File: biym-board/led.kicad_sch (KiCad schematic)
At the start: 0 parts

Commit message: Wire led sheet
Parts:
- added J?: HEADER_01X04_JST_PH_VERTICAL, Janelia:JST_PH_B4B-PH-K_1x04_P2.00mm_Vertical, symbol Janelia:HEADER_01X04_JST_PH_VERTICAL
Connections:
- new net CKI: J?.3 (Pin_3)
- new net GND: J?.1 (Pin_1)
- new net SDI: J?.2 (Pin_2)
- new net VLED: J?.4 (Pin_4)
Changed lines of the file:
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@@
 (kicad_sch (version 20211123) (generator eeschema)
   (paper "A4")
+  (wire (pts (xy 124.46 88.9) (xy 127 88.9))
+    (stroke (width 0) (type default) (color 0 0 0 0))
+  )
+  (wire (pts (xy 124.46 91.44) (xy 127 91.44))
+    (stroke (width 0) (type default) (color 0 0 0 0))
+  )
+  (wire (pts (xy 124.46 86.36) (xy 127 86.36))
+    (stroke (width 0) (type default) (color 0 0 0 0))
+  )
+  (wire (pts (xy 124.46 93.98) (xy 127 93.98))
+    (stroke (width 0) (type default) (color 0 0 0 0))
+  )
+  (hierarchical_label "VLED" (shape passive) (at 124.46 86.36 180)
+    (effects (font (size 1.27 1.27)) (justify right))
+  )
+  (hierarchical_label "SDI" (shape input) (at 124.46 91.44 180)
+    (effects (font (size 1.27 1.27)) (justify right))
+  )
+  (hierarchical_label "GND" (shape passive) (at 124.46 93.98 180)
+    (effects (font (size 1.27 1.27)) (justify right))
+  )
+  (hierarchical_label "CKI" (shape input) (at 124.46 88.9 180)
+    (effects (font (size 1.27 1.27)) (justify right))
+  )
+  (symbol (lib_id "Janelia:HEADER_01X04_JST_PH_VERTICAL") (at 132.08 90.17 180) (unit 1)
+    (in_bom yes) (on_board yes)
+    (property "Reference" "J?" (id 0) (at 132.08 83.82 0))
+    (property "Value" "HEADER_01X04_JST_PH_VERTICAL" (id 1) (at 134.62 90.17 90))
+    (property "Footprint" "Janelia:JST_PH_B4B-PH-K_1x04_P2.00mm_Vertical" (id 2) (at 132.08 102.87 0)
+      (effects (font (size 1.27 1.27)) hide)
+    )
+    (property "Datasheet" "" (id 3) (at 132.08 91.44 0)
+      (effects (font (size 1.27 1.27)) hide)
+    )
+    (property "Description" "CONN HEADER VERT 4POS 2MM" (id 4) (at 132.08 100.33 0)
+      (effects (font (size 1.27 1.27)) hide)
+    )
+    (property "Manufacturer" "JST Sales America Inc." (id 5) (at 132.08 107.95 0)
+      (effects (font (size 1.27 1.27)) hide)
+    )
+    (property "Manufacturer Part Number" "B4B-PH-K-S(LF)(SN)" (id 6) (at 132.08 105.41 0)
+      (effects (font (size 1.27 1.27)) hide)
+    )
+    (property "Vendor" "Digi-Key" (id 7) (at 132.08 110.49 0)
+      (effects (font (size 1.27 1.27)) hide)
+    )
+    (property "Vendor Part Number" "455-1706-ND" (id 8) (at 132.08 113.03 0)
+      (effects (font (size 1.27 1.27)) hide)
+    )
+    (pin "1")
+    (pin "2")
+    (pin "3")
+    (pin "4")
+  )
 )

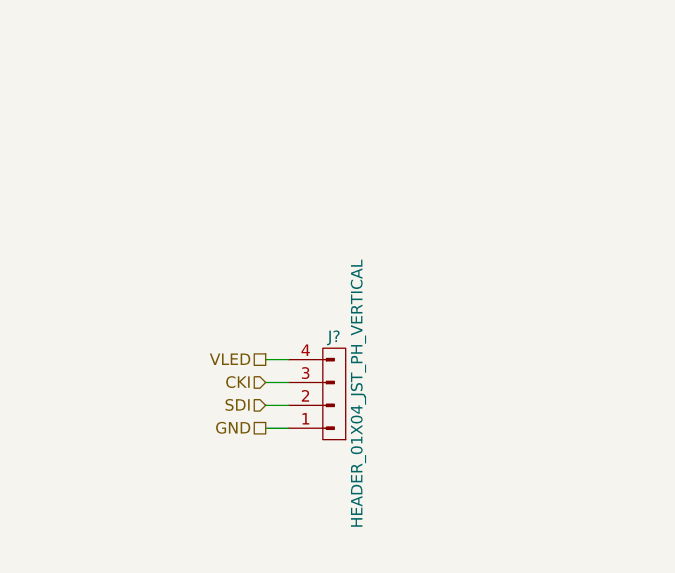
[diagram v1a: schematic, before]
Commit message: Add boosted voltage
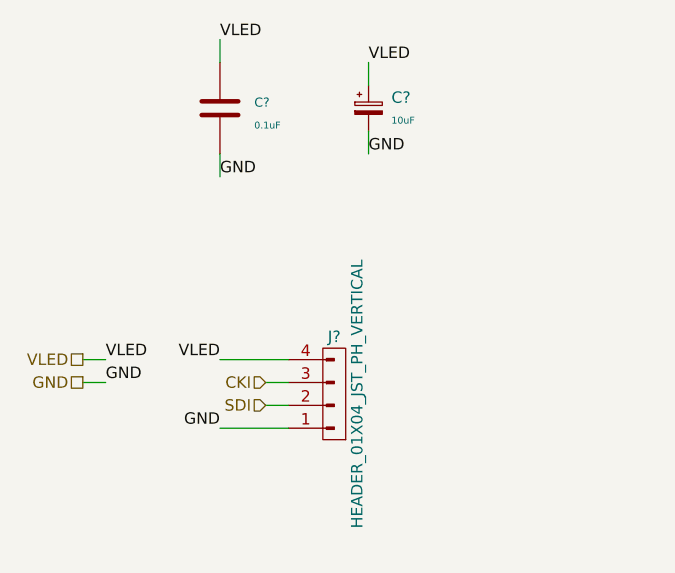
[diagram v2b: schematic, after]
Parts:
- added C?: 0.1uF, Janelia:SM0402, symbol Janelia:0.1uF_0402
- added C?: 10uF, Janelia:SM0402_POL, symbol Janelia:10uF_0402_POL
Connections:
- net GND: now also C?.2, C?.2
- net VLED: now also C?.1, C?.1
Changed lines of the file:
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@@
 (kicad_sch (version 20211123) (generator eeschema)
   (paper "A4")
+  (wire (pts (xy 119.38 63.5) (xy 119.38 66.04))
+    (stroke (width 0) (type default) (color 0 0 0 0))
+  )
+  (wire (pts (xy 135.89 60.96) (xy 135.89 63.5))
+    (stroke (width 0) (type default) (color 0 0 0 0))
+  )
   (wire (pts (xy 124.46 88.9) (xy 127 88.9))
+    (stroke (width 0) (type default) (color 0 0 0 0))
+  )
+  (wire (pts (xy 135.89 53.34) (xy 135.89 55.88))
+    (stroke (width 0) (type default) (color 0 0 0 0))
+  )
+  (wire (pts (xy 104.14 88.9) (xy 106.68 88.9))
+    (stroke (width 0) (type default) (color 0 0 0 0))
+  )
+  (wire (pts (xy 104.14 86.36) (xy 106.68 86.36))
     (stroke (width 0) (type default) (color 0 0 0 0))
   )
@@
     (stroke (width 0) (type default) (color 0 0 0 0))
   )
-  (wire (pts (xy 124.46 86.36) (xy 127 86.36))
+  (wire (pts (xy 119.38 50.8) (xy 119.38 53.34))
     (stroke (width 0) (type default) (color 0 0 0 0))
   )
-  (wire (pts (xy 124.46 93.98) (xy 127 93.98))
+  (wire (pts (xy 119.38 86.36) (xy 127 86.36))
     (stroke (width 0) (type default) (color 0 0 0 0))
   )
-  (hierarchical_label "VLED" (shape passive) (at 124.46 86.36 180)
+  (wire (pts (xy 119.38 93.98) (xy 127 93.98))
+    (stroke (width 0) (type default) (color 0 0 0 0))
+  )
+  (label "VLED" (at 135.89 53.34 0)
+    (effects (font (size 1.27 1.27)) (justify left bottom))
+  )
+  (label "VLED" (at 119.38 86.36 180)
+    (effects (font (size 1.27 1.27)) (justify right bottom))
+  )
+  (label "GND" (at 119.38 93.98 180)
+    (effects (font (size 1.27 1.27)) (justify right bottom))
+  )
+  (label "GND" (at 135.89 63.5 0)
+    (effects (font (size 1.27 1.27)) (justify left bottom))
+  )
+  (label "VLED" (at 106.68 86.36 0)
+    (effects (font (size 1.27 1.27)) (justify left bottom))
+  )
+  (label "VLED" (at 119.38 50.8 0)
+    (effects (font (size 1.27 1.27)) (justify left bottom))
+  )
+  (label "GND" (at 119.38 66.04 0)
+    (effects (font (size 1.27 1.27)) (justify left bottom))
+  )
+  (label "GND" (at 106.68 88.9 0)
+    (effects (font (size 1.27 1.27)) (justify left bottom))
+  )
+  (hierarchical_label "VLED" (shape passive) (at 104.14 86.36 180)
     (effects (font (size 1.27 1.27)) (justify right))
   )
@@
     (effects (font (size 1.27 1.27)) (justify right))
   )
-  (hierarchical_label "GND" (shape passive) (at 124.46 93.98 180)
+  (hierarchical_label "GND" (shape passive) (at 104.14 88.9 180)
     (effects (font (size 1.27 1.27)) (justify right))
   )
@@
     (pin "4")
   )
+  (symbol (lib_id "Janelia:0.1uF_0402") (at 119.38 58.42 0) (unit 1)
+    (in_bom yes) (on_board yes) (fields_autoplaced)
+    (property "Reference" "C?" (id 0) (at 123.19 57.785 0)
+      (effects (font (size 1.016 1.016)) (justify left))
+    )
+    (property "Value" "0.1uF" (id 1) (at 123.19 60.325 0)
+      (effects (font (size 0.762 0.762)) (justify left))
+    )
+    (property "Footprint" "Janelia:SM0402" (id 2) (at 120.3452 62.23 0)
+      (effects (font (size 0.762 0.762)) hide)
+    )
+    (property "Datasheet" "" (id 3) (at 119.38 58.42 0)
+      (effects (font (size 1.524 1.524)) hide)
+    )
+    (property "Vendor" "Digi-Key" (id 4) (at 121.92 53.34 0)
+      (effects (font (size 1.524 1.524)) hide)
+    )
+    (property "Vendor Part Number" "311-1375-1-ND" (id 5) (at 124.46 50.8 0)
+      (effects (font (size 1.524 1.524)) hide)
+    )
+    (property "Description" "CAP CER 0.1UF 25V Y5V" (id 6) (at 127 48.26 0)
+      (effects (font (size 1.524 1.524)) hide)
+    )
+    (property "Package" "0402" (id 7) (at 119.38 58.42 0)
+      (effects (font (size 1.27 1.27)) hide)
+    )
+    (property "Manufacturer" "Yageo" (id 8) (at 119.38 58.42 0)
+      (effects (font (size 1.27 1.27)) hide)
+    )
+    (property "Manufacturer Part Number" "CC0402ZRY5V8BB104" (id 9) (at 119.38 58.42 0)
+      (effects (font (size 1.27 1.27)) hide)
+    )
+    (pin "1")
+    (pin "2")
+  )
+  (symbol (lib_id "Janelia:10uF_0402_POL") (at 135.89 58.42 0) (unit 1)
+    (in_bom yes) (on_board yes) (fields_autoplaced)
+    (property "Reference" "C?" (id 0) (at 138.43 57.2388 0)
+      (effects (font (size 1.27 1.27)) (justify left))
+    )
+    (property "Value" "10uF" (id 1) (at 138.43 59.7789 0)
+      (effects (font (size 0.762 0.762)) (justify left))
+    )
+    (property "Footprint" "Janelia:SM0402_POL" (id 2) (at 133.604 59.182 0)
+      (effects (font (size 1.524 1.524)) hide)
+    )
+    (property "Datasheet" "" (id 3) (at 136.144 56.642 0)
+      (effects (font (size 1.524 1.524)) hide)
+    )
+    (property "Vendor" "Digi-Key" (id 4) (at 138.684 54.102 0)
+      (effects (font (size 1.524 1.524)) hide)
+    )
+    (property "Vendor Part Number" "478-5343-1-ND" (id 5) (at 141.224 51.562 0)
+      (effects (font (size 1.524 1.524)) hide)
+    )
+    (property "Description" "CAP TANT 10UF 20% 6.3V" (id 6) (at 143.764 49.022 0)
+      (effects (font (size 1.524 1.524)) hide)
+    )
+    (property "Manufacturer" "AVX Corporation" (id 7) (at 135.89 58.42 0)
+      (effects (font (size 1.27 1.27)) hide)
+    )
+    (property "Manufacturer Part Number" "TLCK106M006QTA" (id 8) (at 135.89 58.42 0)
+      (effects (font (size 1.27 1.27)) hide)
+    )
+    (property "Package" "0402" (id 9) (at 135.89 58.42 0)
+      (effects (font (size 1.27 1.27)) hide)
+    )
+    (pin "1")
+    (pin "2")
+  )
 )

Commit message: output -> servo
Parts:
- removed J?: HEADER_01X04_JST_PH_VERTICAL, Janelia:JST_PH_B4B-PH-K_1x04_P2.00mm_Vertical, symbol Janelia:HEADER_01X04_JST_PH_VERTICAL
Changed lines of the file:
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@@
     (effects (font (size 1.27 1.27)) (justify right))
-  )
-  (symbol (lib_id "Janelia:HEADER_01X04_JST_PH_VERTICAL") (at 132.08 90.17 180) (unit 1)
-    (in_bom yes) (on_board yes)
-    (property "Reference" "J?" (id 0) (at 132.08 83.82 0))
-    (property "Value" "HEADER_01X04_JST_PH_VERTICAL" (id 1) (at 134.62 90.17 90))
-    (property "Footprint" "Janelia:JST_PH_B4B-PH-K_1x04_P2.00mm_Vertical" (id 2) (at 132.08 102.87 0)
-      (effects (font (size 1.27 1.27)) hide)
-    )
-    (property "Datasheet" "" (id 3) (at 132.08 91.44 0)
-      (effects (font (size 1.27 1.27)) hide)
-    )
-    (property "Description" "CONN HEADER VERT 4POS 2MM" (id 4) (at 132.08 100.33 0)
-      (effects (font (size 1.27 1.27)) hide)
-    )
-    (property "Manufacturer" "JST Sales America Inc." (id 5) (at 132.08 107.95 0)
-      (effects (font (size 1.27 1.27)) hide)
-    )
-    (property "Manufacturer Part Number" "B4B-PH-K-S(LF)(SN)" (id 6) (at 132.08 105.41 0)
-      (effects (font (size 1.27 1.27)) hide)
-    )
-    (property "Vendor" "Digi-Key" (id 7) (at 132.08 110.49 0)
-      (effects (font (size 1.27 1.27)) hide)
-    )
-    (property "Vendor Part Number" "455-1706-ND" (id 8) (at 132.08 113.03 0)
-      (effects (font (size 1.27 1.27)) hide)
-    )
-    (pin "1")
-    (pin "2")
-    (pin "3")
-    (pin "4")
   )
   (symbol (lib_id "Janelia:0.1uF_0402") (at 119.38 58.42 0) (unit 1)

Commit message: Finished v0.1 of schematic
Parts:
- removed C?: 0.1uF, Janelia:SM0402, symbol Janelia:0.1uF_0402
- removed C?: 10uF, Janelia:SM0402_POL, symbol Janelia:10uF_0402_POL
- added C12: C_0.1uF_0402, Janelia:SM0402, symbol Janelia:C_0.1uF_0402
- added C13: C_10uF_0402_POL, Janelia:SM0402_POL, symbol Janelia:C_10uF_0402_POL
- added J3: HEADER_01X04_JST_ZH_SMD_VERTICAL, Janelia:JST_ZH_B4B_ZR_SM4_TF_1x04-1MP_P1.50mm_Vertical, symbol Janelia:HEADER_01X04_JST_ZH_SMD_VERTICAL
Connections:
- net CKI: now also J3.3 (Pin_3)
- net GND: now also C12.2, C13.2, J3.1 (Pin_1)
- net SDI: now also J3.2 (Pin_2)
- net VLED: now also C12.1, C13.1, J3.4 (Pin_4)
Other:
- company: (none) -> Peter Polidoro
- title: (none) -> biym-board-led
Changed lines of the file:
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@@
 (kicad_sch (version 20211123) (generator eeschema)
   (paper "A4")
+  (title_block
+    (title "biym-board-led")
+    (date "2022-11-17")
+    (rev "0.1")
+    (company "Peter Polidoro")
+  )
   (wire (pts (xy 119.38 63.5) (xy 119.38 66.04))
     (stroke (width 0) (type default) (color 0 0 0 0))
@@
     (effects (font (size 1.27 1.27)) (justify right))
   )
-  (symbol (lib_id "Janelia:0.1uF_0402") (at 119.38 58.42 0) (unit 1)
-    (in_bom yes) (on_board yes) (fields_autoplaced)
-    (property "Reference" "C?" (id 0) (at 123.19 57.785 0)
+  (symbol (lib_id "Janelia:HEADER_01X04_JST_ZH_SMD_VERTICAL") (at 132.08 90.17 180) (unit 1)
+    (in_bom yes) (on_board yes)
+    (property "Reference" "J3" (id 0) (at 132.08 83.82 0))
+    (property "Value" "HEADER_01X04_JST_ZH_SMD_VERTICAL" (id 1) (at 132.08 96.52 0))
+    (property "Footprint" "Janelia:JST_ZH_B4B_ZR_SM4_TF_1x04-1MP_P1.50mm_Vertical" (id 2) (at 132.08 102.87 0)
+      (effects (font (size 1.27 1.27)) hide)
+    )
+    (property "Datasheet" "" (id 3) (at 132.08 91.44 0)
+      (effects (font (size 1.27 1.27)) hide)
+    )
+    (property "Description" "CONN HEADER SMD 4POS 1.5MM" (id 4) (at 132.08 100.33 0)
+      (effects (font (size 1.27 1.27)) hide)
+    )
+    (property "Manufacturer" "JST Sales America Inc." (id 5) (at 132.08 107.95 0)
+      (effects (font (size 1.27 1.27)) hide)
+    )
+    (property "Manufacturer Part Number" "B4B-ZR-SM4-TF(LF)(SN)" (id 6) (at 132.08 105.41 0)
+      (effects (font (size 1.27 1.27)) hide)
+    )
+    (property "Vendor" "Digi-Key" (id 7) (at 132.08 110.49 0)
+      (effects (font (size 1.27 1.27)) hide)
+    )
+    (property "Vendor Part Number" "455-1683-1-ND" (id 8) (at 132.08 113.03 0)
+      (effects (font (size 1.27 1.27)) hide)
+    )
+    (pin "1")
+    (pin "2")
+    (pin "3")
+    (pin "4")
+  )
+  (symbol (lib_id "Janelia:C_0.1uF_0402") (at 119.38 58.42 0) (unit 1)
+    (in_bom yes) (on_board yes)
+    (property "Reference" "C12" (id 0) (at 121.92 55.88 0)
       (effects (font (size 1.016 1.016)) (justify left))
     )
-    (property "Value" "0.1uF" (id 1) (at 123.19 60.325 0)
+    (property "Value" "C_0.1uF_0402" (id 1) (at 121.92 58.42 0)
       (effects (font (size 0.762 0.762)) (justify left))
     )
@@
     (pin "2")
   )
-  (symbol (lib_id "Janelia:10uF_0402_POL") (at 135.89 58.42 0) (unit 1)
-    (in_bom yes) (on_board yes) (fields_autoplaced)
-    (property "Reference" "C?" (id 0) (at 138.43 57.2388 0)
+  (symbol (lib_id "Janelia:C_10uF_0402_POL") (at 135.89 58.42 0) (unit 1)
+    (in_bom yes) (on_board yes)
+    (property "Reference" "C13" (id 0) (at 137.16 55.88 0)
       (effects (font (size 1.27 1.27)) (justify left))
     )
-    (property "Value" "10uF" (id 1) (at 138.43 59.7789 0)
+    (property "Value" "C_10uF_0402_POL" (id 1) (at 138.43 58.42 0)
       (effects (font (size 0.762 0.762)) (justify left))
     )
